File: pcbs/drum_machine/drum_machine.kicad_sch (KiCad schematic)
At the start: 128 parts, among them Q1 NPN, Q10 NPN, Q11 NPN, Q12 NPN, Q13 NPN, Q14 NPN, Q15 NPN, Q16 NPN, Q2 NPN, Q3 NPN, Q4 NPN, Q5 NPN, Q6 NPN, Q7 NPN, Q8 NPN, Q9 NPN, SW1 SW_SPDT, SW10 SW_SPDT, SW11 SW_SPDT, SW12 SW_SPDT, SW13 SW_SPDT, SW14 SW_SPDT, SW15 SW_SPDT, SW16 SW_SPDT, SW17 SW_SPDT, SW18 SW_SPDT, SW19 SW_SPDT, SW2 SW_SPDT, SW20 SW_SPDT, SW21 SW_SPDT, SW22 SW_SPDT, SW23 SW_SPDT, SW24 SW_SPDT, SW25 SW_SPDT, SW26 SW_SPDT, SW27 SW_SPDT, SW28 SW_SPDT, SW29 SW_SPDT, SW3 SW_SPDT, SW30 SW_SPDT, SW31 SW_SPDT, SW32 SW_SPDT, SW33 SW_SPDT, SW34 SW_SPDT, SW35 SW_SPDT, SW36 SW_SPDT, SW37 SW_SPDT, SW38 SW_SPDT, SW39 SW_SPDT, SW4 SW_SPDT, SW40 SW_SPDT, SW41 SW_SPDT, SW42 SW_SPDT, SW43 SW_SPDT, SW44 SW_SPDT, SW45 SW_SPDT, SW46 SW_SPDT, SW47 SW_SPDT, SW48 SW_SPDT, SW49 SW_SPDT_CYMBAL, SW5 SW_SPDT, SW50 SW_SPDT_COUNTOFF, SW51 SW_SPDT_PLAYSTOP, SW52 SW_SPDT_LEDS, SW53 SW_SPDT_TIMESIG, SW54 SW_SPDT_RESERVED0, SW55 SW_SPDT_RESERVED1, SW56 SW_SPDT_RESERVED2, SW6 SW_SPDT, SW7 SW_SPDT, SW8 SW_SPDT, SW9 SW_SPDT, U1 CD4051B, U10 CD4051B, U11 CD4051B, U12 CD4051B, U2 Pico, U3 CD4051B, U4 CD4051B, U5 CD4051B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

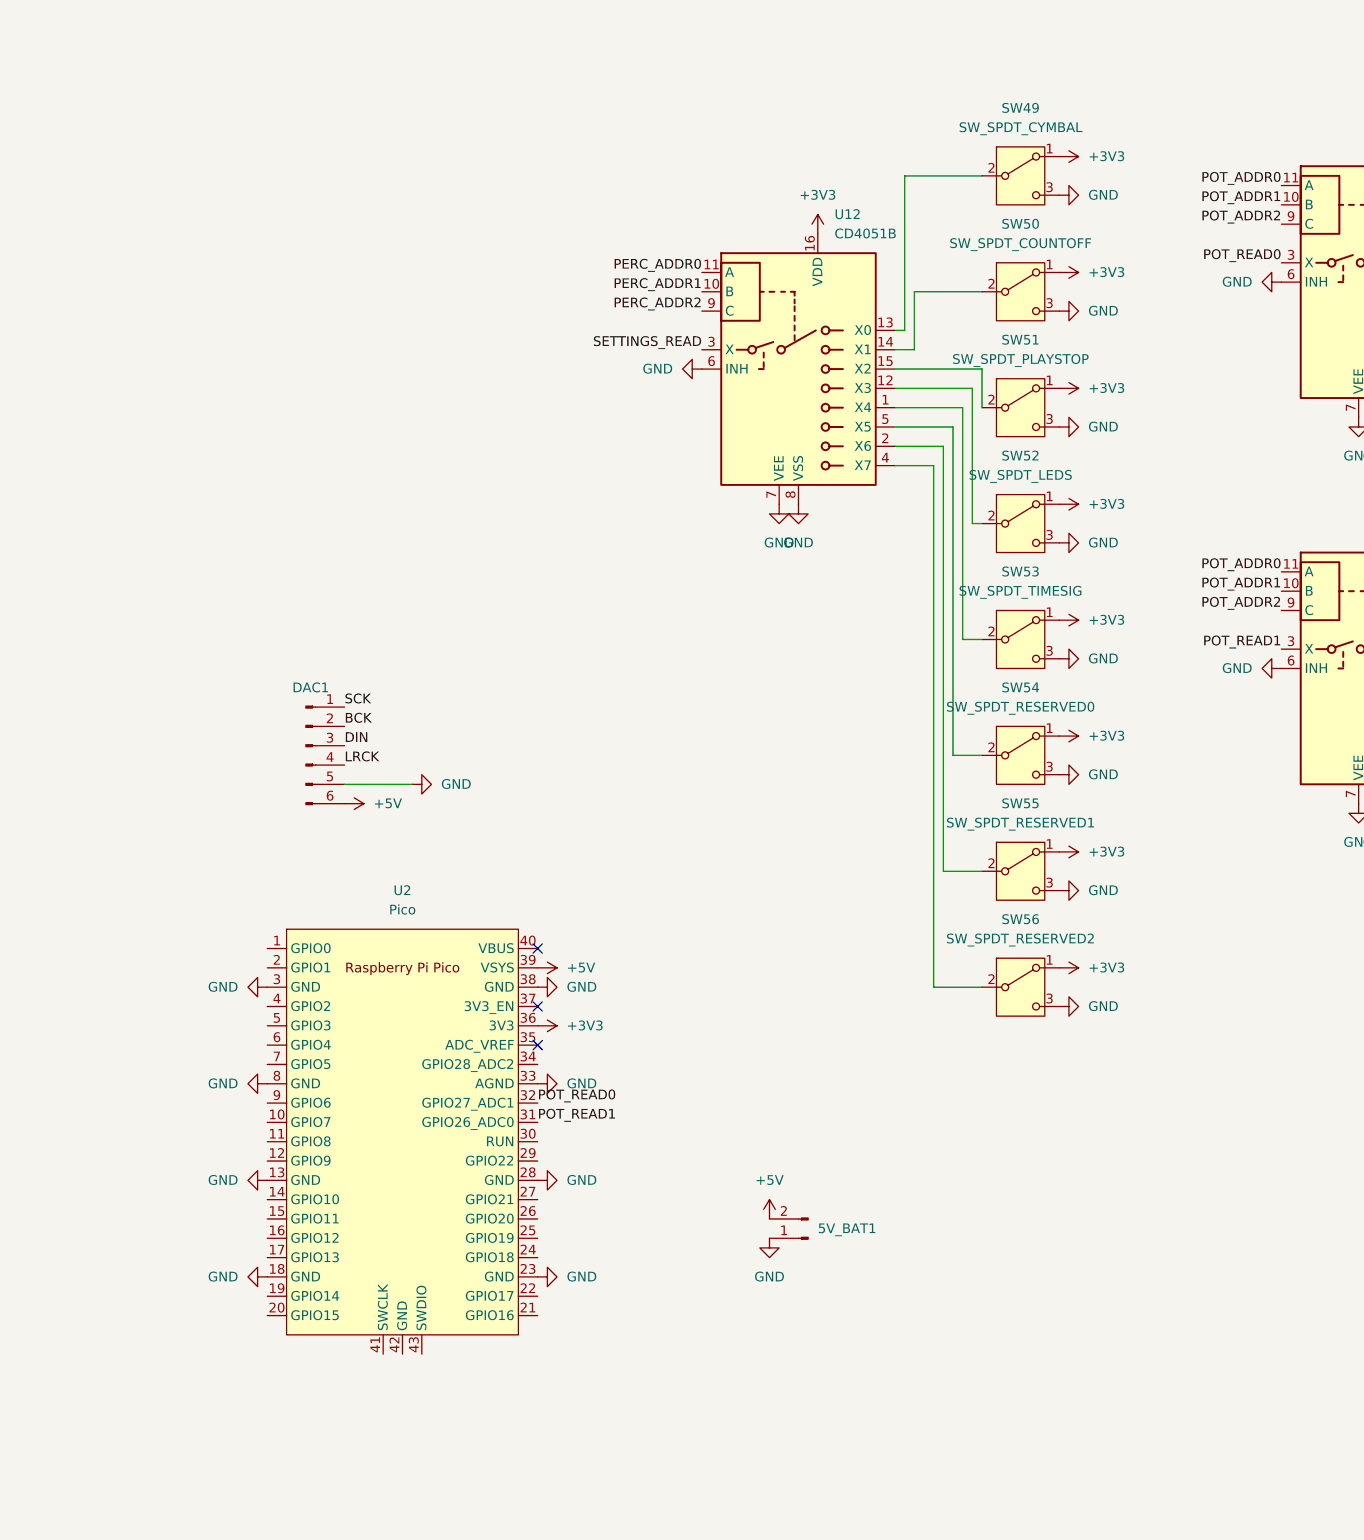
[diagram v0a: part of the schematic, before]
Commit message: Route drum machine
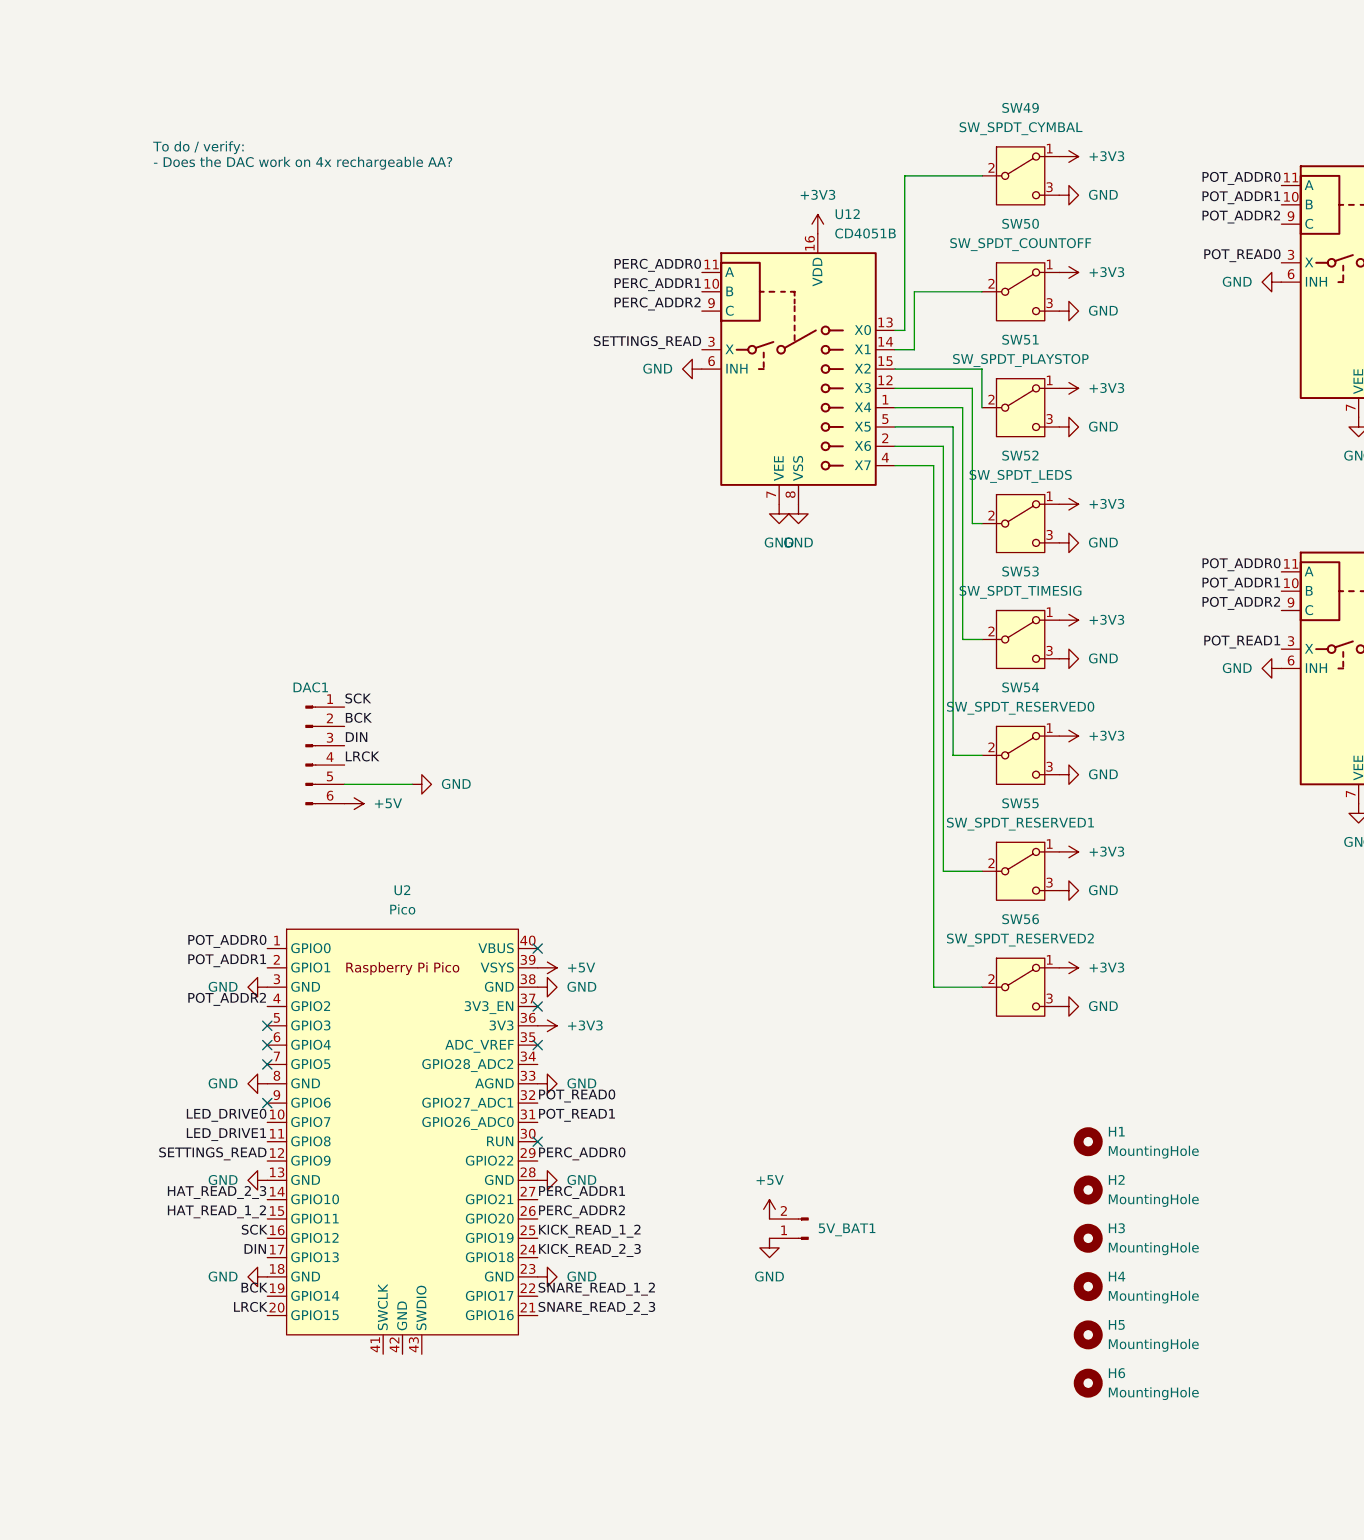
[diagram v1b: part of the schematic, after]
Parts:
- added H1, H2, H3, H4, H5, H6: MountingHole, MountingHole:MountingHole_2.7mm_M2.5, symbol Mechanical:MountingHole
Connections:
- net BCK: now also U2.19 (GPIO14)
- net DIN: now also U2.17 (GPIO13)
- net HAT_READ_1_2: now also U2.15 (GPIO11)
- net HAT_READ_2_3: now also U2.14 (GPIO10)
- net KICK_READ_1_2: now also U2.25 (GPIO19)
- net KICK_READ_2_3: now also U2.24 (GPIO18)
- net LED_DRIVE0: now also U2.10 (GPIO7)
- net LED_DRIVE1: now also U2.11 (GPIO8)
- net LRCK: now also U2.20 (GPIO15)
- net PERC_ADDR0: now also U2.29 (GPIO22)
- net PERC_ADDR1: now also U2.27 (GPIO21)
- net PERC_ADDR2: now also U2.26 (GPIO20)
- net POT_ADDR0: now also U2.1 (GPIO0)
- net POT_ADDR1: now also U2.2 (GPIO1)
- net POT_ADDR2: now also U2.4 (GPIO2)
- net SCK: now also U2.16 (GPIO12)
- net SETTINGS_READ: now also U2.12 (GPIO9)
- net SNARE_READ_1_2: now also U2.22 (GPIO17)
- net SNARE_READ_2_3: now also U2.21 (GPIO16)
- no-connect marks 18 -> 23
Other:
- note added: "To do / verify: - Does the DAC work on 4x rechargeable AA?"

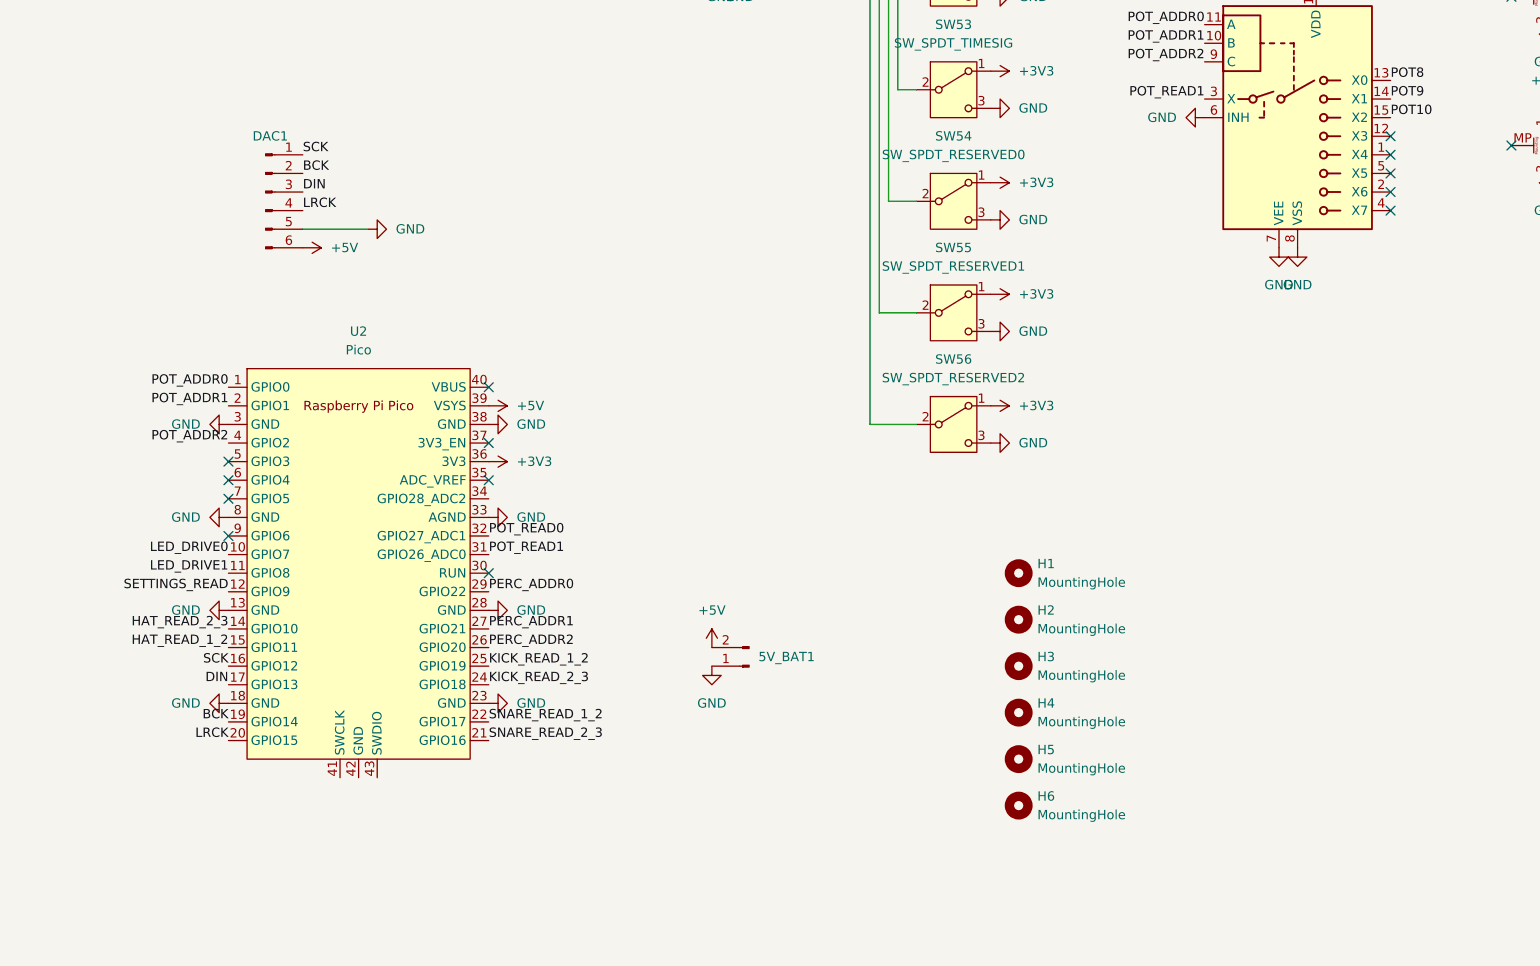
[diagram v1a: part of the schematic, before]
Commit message: Connect LED addresses
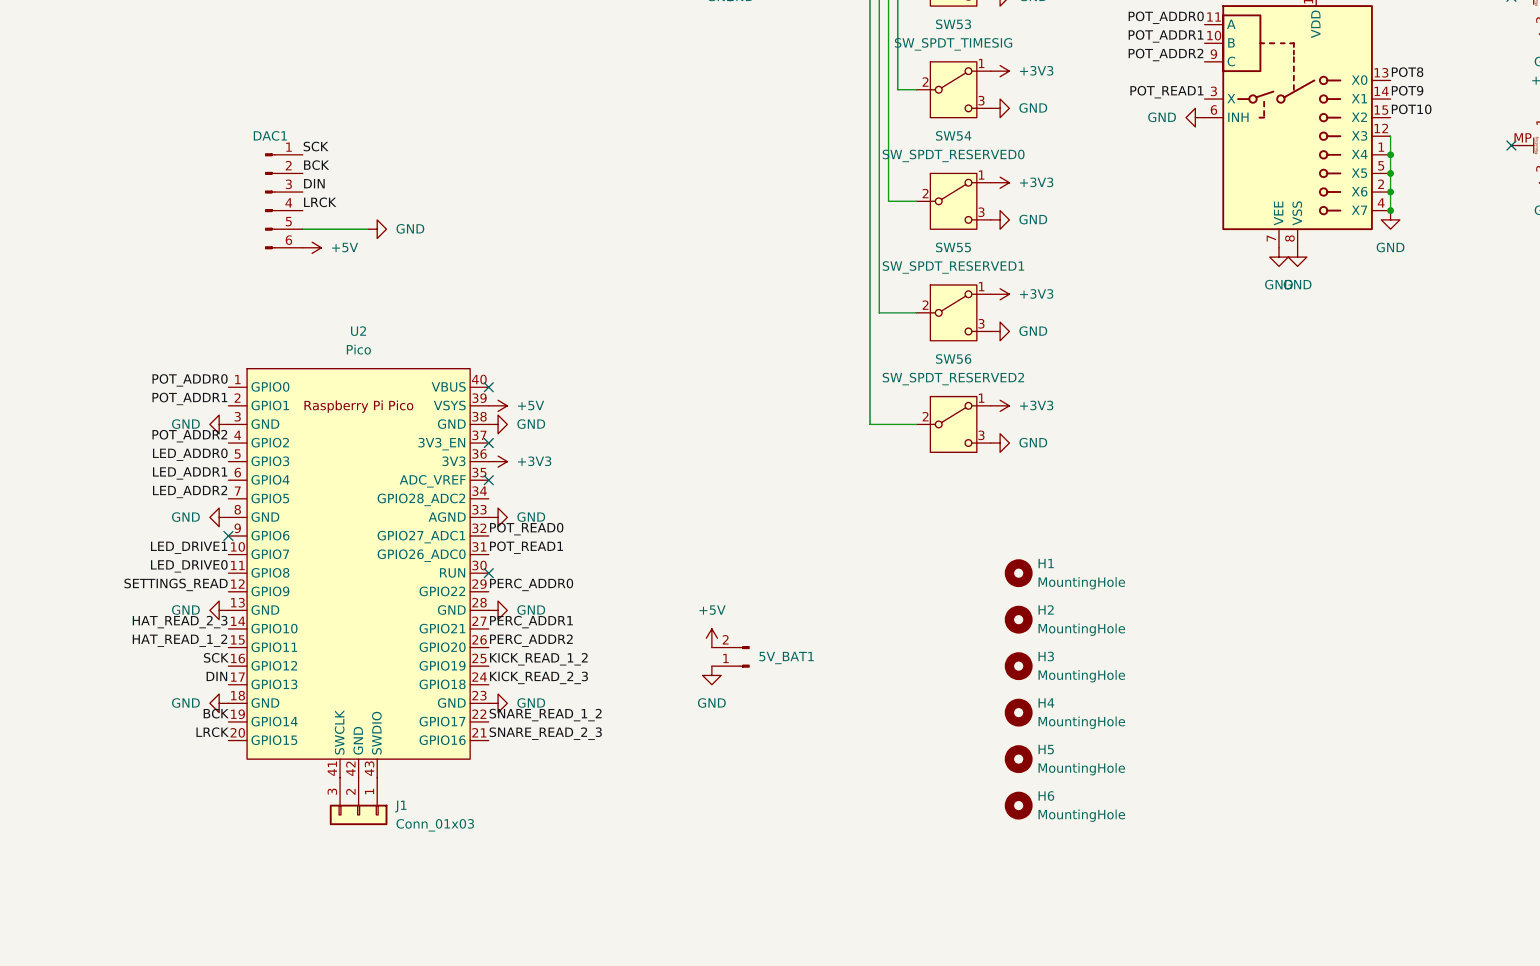
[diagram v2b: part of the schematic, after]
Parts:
- added J1: Conn_01x03, Connector_PinSocket_2.54mm:PinSocket_1x03_P2.54mm_Vertical, symbol Connector_Generic:Conn_01x03
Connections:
- net GND: now also U3.1 (X4), U3.12 (X3), U3.2 (X6), U3.4 (X7), U3.5 (X5)
- net LED_ADDR0: now also U2.5 (GPIO3)
- net LED_ADDR1: now also U2.6 (GPIO4)
- net LED_ADDR2: now also U2.7 (GPIO5)
- net LED_DRIVE0: now also U2.11 (GPIO8); no longer U2.10 (GPIO7)
- net LED_DRIVE1: now also U2.10 (GPIO7); no longer U2.11 (GPIO8)
- net at U2.41 (SWCLK): now also J1.3 (Pin_3)
- net at U2.42 (GND): now also J1.2 (Pin_2)
- net at U2.43 (SWDIO): now also J1.1 (Pin_1)
- no-connect marks 23 -> 15
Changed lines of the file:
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@@
 	(generator_version "8.0")
 	(paper "A4")
+	(junction
+		(at 195.58 96.52)
+		(diameter 0)
+		(color 0 0 0 0)
+	)
+	(junction
+		(at 195.58 101.6)
+		(diameter 0)
+		(color 0 0 0 0)
+	)
+	(junction
+		(at 195.58 104.14)
+		(diameter 0)
+		(color 0 0 0 0)
+	)
+	(junction
+		(at 195.58 99.06)
+		(diameter 0)
+		(color 0 0 0 0)
+	)
 	(no_connect
 		(at 212.09 95.25)
@@
 	)
 	(no_connect
-		(at 36.83 138.43)
-	)
-	(no_connect
 		(at 72.39 135.89)
 	)
 	(no_connect
-		(at 195.58 93.98)
-	)
-	(no_connect
 		(at 212.09 74.93)
 	)
@@
 	)
 	(no_connect
-		(at 36.83 143.51)
-	)
-	(no_connect
-		(at 195.58 99.06)
-	)
-	(no_connect
 		(at 256.54 53.34)
 	)
@@
 	)
 	(no_connect
-		(at 195.58 104.14)
-	)
-	(no_connect
 		(at 233.68 74.93)
 	)
@@
 	)
 	(no_connect
-		(at 36.83 140.97)
-	)
-	(no_connect
-		(at 195.58 101.6)
-	)
-	(no_connect
-		(at 195.58 96.52)
-	)
-	(no_connect
 		(at 72.39 128.27)
 	)
@@
 	(wire
 		(pts
+			(xy 195.58 101.6) (xy 195.58 104.14)
+		)
+		(stroke
+			(width 0)
+			(type default)
+		)
+	)
+	(wire
+		(pts
 			(xy 128.27 87.63) (xy 130.81 87.63)
 		)
@@
 	(wire
 		(pts
+			(xy 195.58 96.52) (xy 195.58 99.06)
+		)
+		(stroke
+			(width 0)
+			(type default)
+		)
+	)
+	(wire
+		(pts
+			(xy 195.58 93.98) (xy 195.58 96.52)
+		)
+		(stroke
+			(width 0)
+			(type default)
+		)
+	)
+	(wire
+		(pts
 			(xy 127 102.87) (xy 127 59.69)
 		)
@@
 	(wire
 		(pts
+			(xy 195.58 99.06) (xy 195.58 101.6)
+		)
+		(stroke
+			(width 0)
+			(type default)
+		)
+	)
+	(wire
+		(pts
 			(xy 125.73 118.11) (xy 130.81 118.11)
 		)
@@
 	)
 	(label "LED_DRIVE0"
-		(at 36.83 151.13 180)
+		(at 36.83 153.67 180)
 		(fields_autoplaced yes)
 		(effects
@@
 		)
 	)
+	(label "LED_ADDR1"
+		(at 36.83 140.97 180)
+		(fields_autoplaced yes)
+		(effects
+			(font
+				(size 1.27 1.27)
+			)
+			(justify right bottom)
+		)
+	)
 	(label "LED_ADDR2"
 		(at 398.78 120.65 180)
@@
 	)
 	(label "LED_DRIVE1"
-		(at 36.83 153.67 180)
+		(at 36.83 151.13 180)
 		(fields_autoplaced yes)
 		(effects
@@
 		)
 	)
+	(label "LED_ADDR0"
+		(at 36.83 138.43 180)
+		(fields_autoplaced yes)
+		(effects
+			(font
+				(size 1.27 1.27)
+			)
+			(justify right bottom)
+		)
+	)
 	(label "HAT_READ_2_3"
 		(at -30.48 342.9 180)
@@
 		)
 	)
+	(label "LED_ADDR2"
+		(at 36.83 143.51 180)
+		(fields_autoplaced yes)
+		(effects
+			(font
+				(size 1.27 1.27)
+			)
+			(justify right bottom)
+		)
+	)
 	(label "KICK_1"
 		(at -124.46 292.1 0)
@@
 	)
 	(symbol
+		(lib_id "Connector_Generic:Conn_01x03")
+		(at 54.61 186.69 270)
+		(unit 1)
+		(exclude_from_sim no)
+		(in_bom yes)
+		(on_board yes)
+		(dnp no)
+		(fields_autoplaced yes)
+		(property "Reference" "J1"
+			(at 59.69 185.4199 90)
+			(effects
+				(font
+					(size 1.27 1.27)
+				)
+				(justify left)
+			)
+		)
+		(property "Value" "Conn_01x03"
+			(at 59.69 187.9599 90)
+			(effects
+				(font
+					(size 1.27 1.27)
+				)
+				(justify left)
+			)
+		)
+		(property "Footprint" "Connector_PinSocket_2.54mm:PinSocket_1x03_P2.54mm_Vertical"
+			(at 54.61 186.69 0)
+			(effects
+				(font
+					(size 1.27 1.27)
+				)
+				(hide yes)
+			)
+		)
+		(property "Datasheet" "~"
+			(at 54.61 186.69 0)
+			(effects
+				(font
+					(size 1.27 1.27)
+				)
+				(hide yes)
+			)
+		)
+		(property "Description" "Generic connector, single row, 01x03, script generated (kicad-library-utils/schlib/autogen/connector/)"
+			(at 54.61 186.69 0)
+			(effects
+				(font
+					(size 1.27 1.27)
+				)
+				(hide yes)
+			)
+		)
+		(pin "1"
+		)
+		(pin "2"
+		)
+		(pin "3"
+		)
+		(instances
+			(project ""
+				(path "/6fe6e81f-96c8-442f-ba68-165a537670bb"
+					(reference "J1")
+					(unit 1)
+				)
+			)
+		)
+	)
+	(symbol
 		(lib_id "Simulation_SPICE:NPN")
 		(at 340.36 26.67 90)
@@
 					(unit 1)
 				)
+			)
+		)
+	)
+	(symbol
+		(lib_id "power:GND")
+		(at 195.58 104.14 0)
+		(unit 1)
+		(exclude_from_sim no)
+		(in_bom yes)
+		(on_board yes)
+		(dnp no)
+		(fields_autoplaced yes)
+		(property "Reference" "#PWR0223"
+			(at 195.58 110.49 0)
+			(effects
+				(font
+					(size 1.27 1.27)
+				)
+				(hide yes)
+			)
+		)
+		(property "Value" "GND"
+			(at 195.58 109.22 0)
+			(effects
+				(font
+					(size 1.27 1.27)
+				)
+			)
+		)
+		(property "Footprint" ""
+			(at 195.58 104.14 0)
+			(effects
+				(font
+					(size 1.27 1.27)
+				)
+				(hide yes)
+			)
+		)
+		(property "Datasheet" ""
+			(at 195.58 104.14 0)
+			(effects
+				(font
+					(size 1.27 1.27)
+				)
+				(hide yes)
+			)
+		)
+		(property "Description" "Power symbol creates a global label with name \"GND\" , ground"
+			(at 195.58 104.14 0)
+			(effects
+				(font
+					(size 1.27 1.27)
+				)
+				(hide yes)
+			)
+		)
+		(pin "1"
+		)
+		(instances
+			(project "drum_machine"
+				(path "/6fe6e81f-96c8-442f-ba68-165a537670bb"
+					(reference "#PWR0223")
+					(unit 1)
+				)

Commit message: Add drum machine software
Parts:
- R1, R10, R11, R12, R13, R14, R15, R16, R2, R3, R4, R5, R6, R7, R8, R9: footprint (none) -> Resistor_THT:R_Axial_DIN0207_L6.3mm_D2.5mm_P7.62mm_Horizontal
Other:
- note added: "To do / verify: x Does the DAC work on 4x rechargeable AA?"
- note removed: "To do / verify: - Does the DAC work on 4x rechargeable AA?"
